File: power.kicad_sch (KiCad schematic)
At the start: 26 parts, among them J4 USB_C_Receptacle_USB2.0_16P, SW2 Slide_DPDT_SS22D06, U2 TPS7A0333PDBVR, U3 MCP73831T-2ACI/OT

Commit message: mariposa v2 RC2
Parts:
- removed RN1: 2x R22, PCM_Resistor_SMD_AKL:R_Array_Convex_2x0402, symbol PCM_Resistor_US_AKL:R_2x0402_Convex
- added C4, C5: 10nF, Capacitor_SMD:C_0402_1005Metric, symbol PCM_Elektuur:C
- added D4: D_Schottky, PCM_Diode_SMD_Handsoldering_AKL:D_SOD-123F, symbol Device:D_Schottky
- added FB5: 120 Ohm, PCM_Ferrite_SMD_AKL:Ferrite_0805_2012Metric, symbol PCM_Device_AKL:Ferrite_Bead
- added FB6, FB7: 240 Ohm, PCM_Ferrite_SMD_AKL:Ferrite_0603_1608Metric, symbol PCM_Device_AKL:Ferrite_Bead
- added J7: Ext VCC Out, Connector_JST:JST_SUR_SM02B-SURS-TF_1x02-1MP_P0.80mm_Horizontal, symbol Connector_Generic_MountingPin:Conn_01x02_MountingPin
- BT1: footprint Connector_JST:JST_PH_S2B-PH-SM4-TB_1x02-1MP_P2.00mm_Horizontal -> Connector_JST:JST_GH_SM02B-GHS-TB_1x02-1MP_P1.25mm_Horizontal; symbol Device:Battery_Cell -> Connector_Generic_MountingPin:Conn_01x02_MountingPin
- C46, C47: footprint Capacitor_SMD:C_0805_2012Metric -> Capacitor_SMD:C_0603_1608Metric
- FB1, FB2: value 60ohm -> 120 Ohm
- R1, R8: footprint Resistor_SMD:R_0805_2012Metric -> Resistor_SMD:R_0603_1608Metric
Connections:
- net gpio3 is gone; now on net sda: D12.3 (L2)
- net D+: now also D10.4 (L3), J4.A6 (D+), J4.B6 (D+)
- net D-: now also D10.3 (L2), J4.A7 (D-), J4.B7 (D-)
- net GND: now also C4.1 (+), C5.1 (+), FB5.1, FB7.2, J7.MP (MountPin); no longer J4.A1 (GND), J4.A12 (GND), J4.B1 (GND), J4.B12 (GND)
- net VBUS: now also C5.2 (-); no longer D9.2 (A)
- net VCC: now also D4.2 (A)
- net cs: now also D11.3 (L2); no longer D11.6 (L4)
- net gpio1: now also D10.1 (L1); no longer D10.6 (L4)
- net gpio2: now also D10.6 (L4); no longer D10.4 (L3)
- net led_data: no longer D13.6 (L4)
- net mosi: now also D11.6 (L4); no longer D11.3 (L2)
- net reset: now also D13.6 (L4); no longer D13.4 (L3)
- net sda: no longer D12.6 (L4)
- net swdclk: now also D13.4 (L3); no longer D13.1 (L1)
- net at FB1.1, J4.A4 (VBUS), J4.A9 (VBUS)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: now also D9.2 (A), C4.2 (-)
- net VDC: now reaches C44.1, D45.1 (K), D88.1 (K), U2.1 (VIN), U2.3 (EN)
- removed net IN_D+: D10.3 (L2), J4.A6 (D+), J4.B6 (D+)
- removed net IN_D-: D10.1 (L1), J4.A7 (D-), J4.B7 (D-)
- net gpio4 renamed status_led_2
- new net: FB5.2, J4.A1 (GND), J4.A12 (GND), J4.B1 (GND), J4.B12 (GND)
- new net: D4.1 (K), FB6.2
- new net Earth_Clean: FB7.1, J7.2 (Pin_2)
- new net PRI_MID: FB6.1, J7.1 (Pin_1)
- new net VDD: D13.1 (L1)
- new net status_led_1: D12.6 (L4)
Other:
- note added: "add-on vcc"
- moved on the sheet: BT1, D88, D9, FB1, R10, R9, SW2A

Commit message: mariposa v2 RC3
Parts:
- removed D4: D_Schottky, PCM_Diode_SMD_Handsoldering_AKL:D_SOD-123F, symbol Device:D_Schottky
- removed FB7: 240 Ohm, PCM_Ferrite_SMD_AKL:Ferrite_0603_1608Metric, symbol PCM_Device_AKL:Ferrite_Bead
- removed R1: 20k, Resistor_SMD:R_0603_1608Metric, symbol Device:R_US
- removed SW2: Slide_DPDT_SS22D06, Button_Switch_SMD:SW_DPDT_CK_JS202011JCQN, symbol PCM_4ms_Switch:Slide_DPDT_SS22D06
- removed U2: TPS7A0333PDBVR, Package_TO_SOT_SMD:SOT-23-5, symbol Regulator_Linear:AP2112K-3.3
- removed U3: MCP73831T-2ACI/OT, Package_TO_SOT_SMD:SOT-23-5, symbol Battery_Management:MCP73831-2-OT
- added D6: LED, coquette_footprints:LED 1206 reverse mount rectangle, symbol Device:LED
- added L1: 1 uH, Inductor_SMD:L_0603_1608Metric, symbol PCM_Generic-50:L,IEEE
- added R11: 249k, Resistor_SMD:R_0603_1608Metric, symbol Device:R_US
- added R12, R14: 10k, Resistor_SMD:R_0603_1608Metric, symbol Device:R_US
- added R15: 27k, Resistor_SMD:R_0603_1608Metric, symbol Device:R_US
- added R7: 1.5k, Resistor_SMD:R_0603_1608Metric, symbol Device:R_US
- added U2: BQ25170DSGR, coquette_footprints:DSG0008A, symbol coquette_symbols:BQ25170DSGR
- added U5: TPS628438DRL, Package_TO_SOT_SMD:SOT-563, symbol Regulator_Switching:TPS628438DRL
- C4, C5: footprint Capacitor_SMD:C_0402_1005Metric -> Capacitor_SMD:C_0603_1608Metric
- C44: value 1uF -> 4.7 uF
- C45: value 1uF -> 10 uF
- C46, C47: value 4.7uF -> 1uF
- D1: footprint PCM_LED_SMD_AKL:LED_1206_3216Metric_ReverseMount_Hole1.8x2.4mm -> coquette_footprints:LED 1206 reverse mount rectangle
- FB6: value 240 Ohm -> 120 Ohm
- R9: value 800K -> 800k
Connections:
- net +3V8 is gone; now on net +BATT: D45.2 (A), R9.1
- net Earth_Clean is gone; now on net GND: J7.2 (Pin_2)
- net VDD is gone; now on net VCC: D13.1 (L1)
- net status_led_2 is gone; now on net led_data: D12.1 (L1)
- net +BATT: now also U2.8 (OUT)
- net D+: now also D10.6 (L4); no longer D10.4 (L3)
- net D-: now also D10.1 (L1); no longer D10.3 (L2)
- net GND: now also R11.2, R12.2, R15.2, R7.2, U2.4 (GND), U2.9 (PAD), U5.1 (GND); no longer R8.2
- net VBUS: now also R8.1, R14.1, U2.1 (IN)
- net VCC: now also FB6.2, L1.2 (-), U5.6 (VOS); no longer D11.1 (L1)
- net VDC: now also U5.2 (VIN), U5.4 (EN)
- net gpio1: now also D10.3 (L2); no longer D10.1 (L1)
- net gpio2: now also D10.4 (L3); no longer D10.6 (L4)
- net at D1.1 (K): now also U2.5 (STAT)
- net at D1.2 (A): now also R8.2
- new net: R7.1, U2.2 (ISET)
- new net: R11.1, U5.3 (VSET)
- new net: L1.1 (+), U5.5 (SW)
- new net: R12.1, U2.3 (TS)
- new net: D6.1 (K), U2.6 (PG_N)
- new net: R15.1, U2.7 (VSET)
- new net: D6.2 (A), R14.2
- no-connect marks 3 -> 2
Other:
- note added: "esd protection tvs arrays"
- note added: "keyboard add-on vcc"
- note removed: "add-on vcc"
- note removed: "power switch"
- moved on the sheet: BT1, C44, C45, C46, C47, D1, D10, D11, D12, D13, D45, D88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

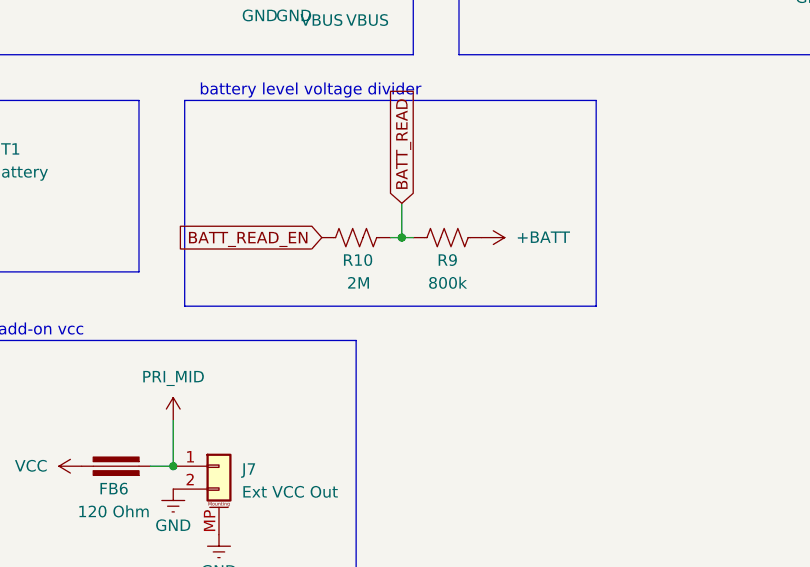
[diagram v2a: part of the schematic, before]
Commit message: another resistor value to a real-world existing part
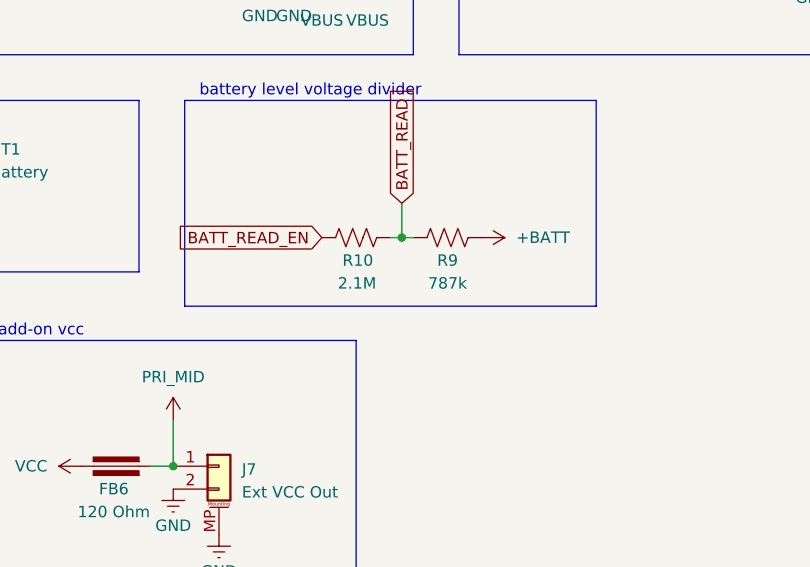
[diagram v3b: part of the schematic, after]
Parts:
- R10: value 2M -> 2.1M
- R9: value 800k -> 787k
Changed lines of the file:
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@@
 			)
 		)
-		(property "Value" "800k"
+		(property "Value" "787k"
 			(at 173.99 92.71 90)
 			(effects
@@
 			)
 		)
-		(property "Value" "2M"
-			(at 162.814 92.71 90)
-			(effects
-				(font
+		(property "Value" "2.1M"
+			(at 161.798 92.71 90)
+			(effects
+				(font

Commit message: actually production version, for real?
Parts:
- FB6: footprint PCM_Ferrite_SMD_AKL:Ferrite_0603_1608Metric -> PCM_Ferrite_SMD_AKL:Ferrite_0805_2012Metric
- R10: value 2.1M -> 2M
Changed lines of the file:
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@@
 			)
 		)
-		(property "Footprint" "PCM_Ferrite_SMD_AKL:Ferrite_0603_1608Metric"
+		(property "Footprint" "PCM_Ferrite_SMD_AKL:Ferrite_0805_2012Metric"
 			(at 137.16 116.332 0)
 			(effects
@@
 			)
 		)
-		(property "Value" "2.1M"
+		(property "Value" "2M"
 			(at 161.798 92.71 90)
 			(effects

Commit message: the final, actual, mk2 production files for real
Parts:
- removed D45: D_Schottky, PCM_Diode_SMD_Handsoldering_AKL:D_SOD-123F, symbol Device:D_Schottky
- added U3: LM66100DCK, Package_TO_SOT_SMD:SOT-363_SC-70-6, symbol Power_Management:LM66100DCK
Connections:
- net +BATT: now also U3.1 (VIN)
- net GND: now also U3.2 (GND), U3.5 (ST)
- net VDC: now also U3.3 (~{CE}), U3.6 (VOUT)
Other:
- note added: "power input select"
- moved on the sheet: C44, C45, D88, FB6, J7, L1, R11, U5

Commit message: mariposa v2 pre
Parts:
- removed D1, D6: LED, coquette_footprints:LED 1206 reverse mount rectangle, symbol Device:LED
- removed D88: D_Schottky, PCM_Diode_SMD_Handsoldering_AKL:D_SOD-123F, symbol Device:D_Schottky
- removed FB5, FB6: 120 Ohm, PCM_Ferrite_SMD_AKL:Ferrite_0805_2012Metric, symbol PCM_Device_AKL:Ferrite_Bead
- removed J7: Ext VCC Out, Connector_JST:JST_SUR_SM02B-SURS-TF_1x02-1MP_P0.80mm_Horizontal, symbol Connector_Generic_MountingPin:Conn_01x02_MountingPin
- removed R14, R8: 10k, Resistor_SMD:R_0603_1608Metric, symbol Device:R_US
- added C6, C7: 1uF, Capacitor_SMD:C_0603_1608Metric, symbol Device:C
- added D14, D2, D3, D4, D7, D8: TPD4E1U06, coquette_footprints:TPD4E1U06, symbol coquette_symbols:TPD4E1U06
- added U6: LM66100DCK, coquette_footprints:LM66100DCK, symbol Power_Management:LM66100DCK
- BT1: footprint Connector_JST:JST_GH_SM02B-GHS-TB_1x02-1MP_P1.25mm_Horizontal -> Connector_Molex:Molex_PicoBlade_53261-0271_1x02-1MP_P1.25mm_Horizontal
- C4, C5: footprint Capacitor_SMD:C_0603_1608Metric -> Capacitor_SMD:C_0402_1005Metric
- D10, D11, D12, D13: footprint PCM_Package_TO_SOT_SMD_AKL:SOT-363_SC-70-6 -> coquette_footprints:TPD4E1U06
- D9: footprint PCM_Diode_SMD_AKL:D_SOD-323_TVS -> coquette_footprints:TSD05C
- FB1, FB2: footprint PCM_Ferrite_SMD_AKL:Ferrite_0805_2012Metric -> PCM_Ferrite_SMD_AKL:Ferrite_1206_3216Metric
- U3: footprint Package_TO_SOT_SMD:SOT-363_SC-70-6 -> coquette_footprints:LM66100DCK
- U5: footprint Package_TO_SOT_SMD:SOT-563 -> coquette_footprints:TPS628438DRL
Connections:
- net led_data is gone; now on net PRI_MID: D12.1 (L1)
- net +BATT: now also C6.1, U6.3 (~{CE})
- net GND: now also J4.A1 (GND), J4.A12 (GND), J4.B1 (GND), J4.B12 (GND), C6.2, C7.2, D14.2 (VN), D14.5 (NC), D2.2 (VN), D2.5 (NC), D3.2 (VN), D3.5 (NC), D4.2 (VN), D4.5 (NC), D7.2 (VN), D7.5 (NC), D8.2 (VN), D8.5 (NC), U6.2 (GND), U6.5 (ST)
- net VBUS: now also U3.3 (~{CE}), C7.1, U6.1 (VIN)
- net VDC: now also U6.6 (VOUT); no longer U3.3 (~{CE})
- net cs: now also D11.1 (L1); no longer D11.3 (L2)
- net LINE: now reaches C4.2 (-), D9.2 (A), FB1.1, J4.A4 (VBUS), J4.A9 (VBUS), J4.B4 (VBUS), J4.B9 (VBUS)
- net chg_stat: now reaches U2.5 (STAT)
- net chg_pg: now reaches U2.6 (PG_N)
- net status_led_1 renamed argb_data_out
- new net ch1: D3.4 (L3)
- new net ch10: D4.1 (L1)
- new net ch11: D2.3 (L2)
- new net ch12: D2.1 (L1)
- new net ch13: D7.4 (L3)
- new net ch14: D7.6 (L4)
- new net ch15: D7.3 (L2)
- new net ch16: D7.1 (L1)
- new net ch17: D8.4 (L3)
- new net ch18: D8.6 (L4)
- new net ch19: D8.1 (L1)
- new net ch2: D3.6 (L4)
- new net ch20: D8.3 (L2)
- new net ch21: D14.3 (L2)
- new net ch22: D14.4 (L3)
- new net ch23: D14.6 (L4)
- new net ch24: D14.1 (L1)
- new net ch3: D3.3 (L2)
- new net ch4: D3.1 (L1)
- new net ch5: D2.4 (L3)
- new net ch6: D2.6 (L4)
- new net ch7: D4.4 (L3)
- new net ch8: D4.6 (L4)
- new net ch9: D4.3 (L2)
- new net eepy: D11.3 (L2)
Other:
- note removed: "keyboard add-on vcc"
- moved on the sheet: BT1, C4, C44, C45, C5, D10, D11, D12, D13, D9, FB1, J4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
